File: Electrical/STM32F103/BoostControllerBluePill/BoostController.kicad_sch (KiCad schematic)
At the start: 60 parts, among them J1 PW-RPM-SPD-TPS, J2 OIL-WATER-AFR, J3 WG-FPUMP, J4 MAP-FPRES, J5 CAN, J6 GND_TP, J7 PROG, Q3 S9013, Q4 S9013, U1 YAAJ_BluePill_SWD_Breakout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

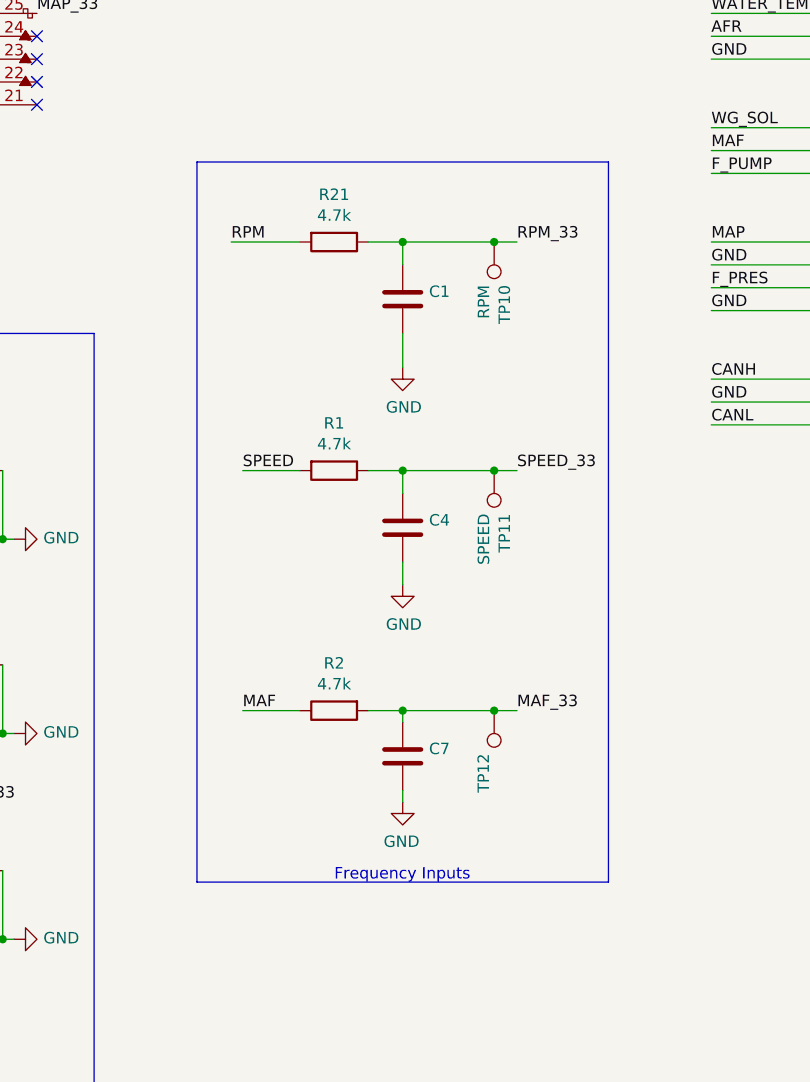
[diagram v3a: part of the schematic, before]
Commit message: [Electrical] Changed  frequency input voltage divider + filter rather than zener diode clamping.
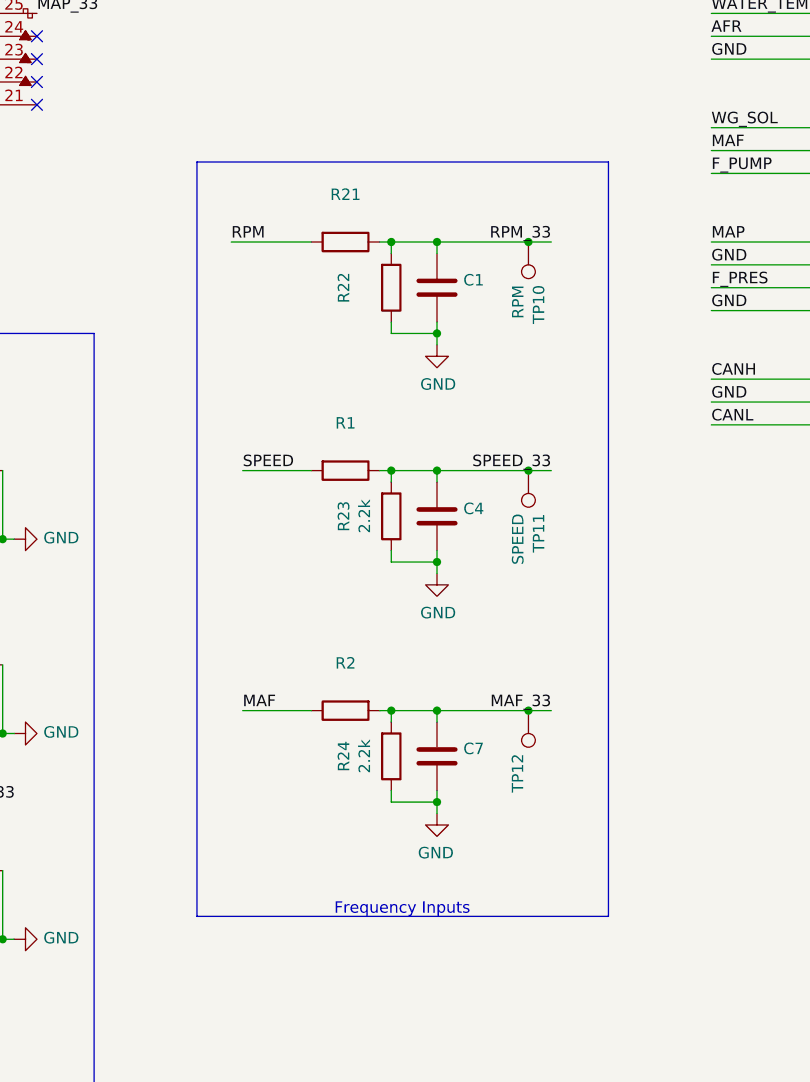
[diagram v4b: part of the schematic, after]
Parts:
- added R22: (no value), symbol Device:R
- added R23, R24: 2.2k, Resistor_SMD:R_1206_3216Metric_Pad1.30x1.75mm_HandSolder, symbol Device:R
- R1, R2, R21: value 4.7k -> (none); footprint Resistor_SMD:R_1206_3216Metric_Pad1.30x1.75mm_HandSolder -> (none)
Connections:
- net GND: now also R22.1, R23.1, R24.1
- net MAF_33: now also R24.2
- net RPM_33: now also R22.2
- net SPEED_33: now also R23.2
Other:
- moved on the sheet: C1, C4, C7, R1, R2, R21, TP10, TP11, TP12

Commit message: Added serial port support on dupond header for local data logging. Added missing MAF input resistor. Changed power transistor reference. Changed analog input voltage divisor values.
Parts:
- added J8: (no value), symbol Connector_Generic:Conn_01x03
- C1, C4, C7: value (none) -> 10n; footprint (none) -> Capacitor_SMD:C_0603_1608Metric_Pad1.08x0.95mm_HandSolder
- C10, C2, C3, C5, C6, C8, C9: value (none) -> 10µ; footprint (none) -> Capacitor_SMD:C_0603_1608Metric_Pad1.08x0.95mm_HandSolder
- Q1, Q2: value (none) -> IRF3205; footprint (none) -> Package_TO_SOT_THT:TO-220-3_Vertical
- R1, R11, R13, R15, R17, R19, R2, R21, R7, R9: value (none) -> 1.2k; footprint (none) -> Resistor_SMD:R_1206_3216Metric_Pad1.30x1.75mm_HandSolder
- R10, R12, R14, R16, R18, R20, R22, R8: value (none) -> 2.2k; footprint (none) -> Resistor_SMD:R_1206_3216Metric_Pad1.30x1.75mm_HandSolder
- TP12: value (none) -> MAF; footprint (none) -> TestPoint:TestPoint_Pad_D3.0mm
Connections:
- net GND: now also J8.2 (Pin_2)
- net TX: now reaches U1.14 (PB6)
- net TX: now also J8.1 (Pin_1)
- net RX: now reaches U1.15 (PB7)
- net RX: now also J8.3 (Pin_3)
- no-connect marks 23 -> 21

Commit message: Added CAN load resistor and jumper
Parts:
- added JP1: CAN load resistor, Connector_PinHeader_2.54mm:PinHeader_1x02_P2.54mm_Vertical, symbol Jumper:Jumper_2_Bridged
- added R25: 120, Resistor_SMD:R_1206_3216Metric_Pad1.30x1.75mm_HandSolder, symbol Device:R
- J8: value (none) -> SERIAL; footprint (none) -> Connector_PinHeader_2.54mm:PinHeader_1x03_P2.54mm_Vertical
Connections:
- net CANH: now also JP1.1 (A)
- net CANL: now also R25.1
- new net: JP1.2 (B), R25.2
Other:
- note added: "Analog Inputs"
- moved on the sheet: U3
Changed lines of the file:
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@@
     (stroke (width 0) (type default) (color 0 0 0 0))
   )
-  (wire (pts (xy 49.53 148.59) (xy 49.53 152.4))
+  (wire (pts (xy 43.18 151.13) (xy 43.18 154.94))
     (stroke (width 0) (type default) (color 0 0 0 0))
   )
@@
     (stroke (width 0) (type default) (color 0 0 0 0))
   )
-  (wire (pts (xy 46.99 148.59) (xy 46.99 152.4))
+  (wire (pts (xy 40.64 151.13) (xy 40.64 154.94))
     (stroke (width 0) (type default) (color 0 0 0 0))
   )
@@
     (stroke (width 0) (type default) (color 0 0 0 0))
   )
+  (wire (pts (xy 76.2 165.1) (xy 76.2 170.18))
+    (stroke (width 0) (type default) (color 0 0 0 0))
+  )
   (wire (pts (xy 153.67 119.38) (xy 163.83 119.38))
     (stroke (width 0) (type default) (color 0 0 0 0))
@@
     (stroke (width 0) (type default) (color 0 0 0 0))
   )
-  (wire (pts (xy 60.96 165.1) (xy 68.58 165.1))
+  (wire (pts (xy 54.61 167.64) (xy 64.77 167.64))
     (stroke (width 0) (type default) (color 0 0 0 0))
   )
@@
     (stroke (width 0) (type default) (color 0 0 0 0))
   )
+  (wire (pts (xy 76.2 170.18) (xy 74.93 170.18))
+    (stroke (width 0) (type default) (color 0 0 0 0))
+  )
   (wire (pts (xy 212.09 148.59) (xy 212.09 149.86))
     (stroke (width 0) (type default) (color 0 0 0 0))
@@
     (stroke (width 0) (type default) (color 0 0 0 0))
   )
+  (wire (pts (xy 67.31 170.18) (xy 64.77 170.18))
+    (stroke (width 0) (type default) (color 0 0 0 0))
+  )
   (wire (pts (xy 49.53 127) (xy 29.21 127))
     (stroke (width 0) (type default) (color 0 0 0 0))
@@
     (stroke (width 0) (type default) (color 0 0 0 0))
   )
-  (wire (pts (xy 26.67 165.1) (xy 35.56 165.1))
+  (wire (pts (xy 20.32 167.64) (xy 29.21 167.64))
     (stroke (width 0) (type default) (color 0 0 0 0))
   )
@@
     (stroke (width 0) (type default) (color 0 0 0 0))
   )
+  (wire (pts (xy 64.77 170.18) (xy 64.77 167.64))
+    (stroke (width 0) (type default) (color 0 0 0 0))
+  )
   (polyline (pts (xy 173.99 191.77) (xy 82.55 191.77))
     (stroke (width 0) (type default) (color 0 0 0 0))
@@
     (stroke (width 0) (type default) (color 0 0 0 0))
   )
-  (wire (pts (xy 26.67 162.56) (xy 35.56 162.56))
+  (wire (pts (xy 20.32 165.1) (xy 29.21 165.1))
     (stroke (width 0) (type default) (color 0 0 0 0))
   )
@@
     (stroke (width 0) (type default) (color 0 0 0 0))
   )
-  (wire (pts (xy 60.96 162.56) (xy 68.58 162.56))
+  (wire (pts (xy 54.61 165.1) (xy 66.04 165.1))
     (stroke (width 0) (type default) (color 0 0 0 0))
   )
@@
   )
   (text "Frequency Inputs" (at 200.66 161.29 0)
+    (effects (font (size 1.27 1.27)) (justify left bottom))
+  )
+  (text "Analog Inputs" (at 121.92 191.77 0)
     (effects (font (size 1.27 1.27)) (justify left bottom))
   )
@@
     (effects (font (size 1.27 1.27)) (justify right bottom))
   )
-  (label "CAN_TX" (at 26.67 162.56 0)
+  (label "CAN_TX" (at 20.32 165.1 0)
     (effects (font (size 1.27 1.27)) (justify left bottom))
   )
@@
     (effects (font (size 1.27 1.27)) (justify left bottom))
   )
-  (label "CANL" (at 68.58 165.1 180)
+  (label "CANL" (at 62.23 167.64 180)
     (effects (font (size 1.27 1.27)) (justify right bottom))
   )
@@
     (effects (font (size 1.27 1.27)) (justify right bottom))
   )
-  (label "+5V" (at 46.99 148.59 90)
+  (label "+5V" (at 40.64 151.13 90)
     (effects (font (size 1.27 1.27)) (justify left bottom))
   )
@@
     (effects (font (size 1.27 1.27)) (justify left bottom))
   )
-  (label "CANH" (at 68.58 162.56 180)
+  (label "CANH" (at 62.23 165.1 180)
     (effects (font (size 1.27 1.27)) (justify right bottom))
   )
-  (label "CAN_RX" (at 26.67 165.1 0)
+  (label "CAN_RX" (at 20.32 167.64 0)
     (effects (font (size 1.27 1.27)) (justify left bottom))
   )
@@
     (pin "1")
   )
-  (symbol (lib_id "BoostController-rescue:MCP2551_MODULE-sonix") (at 48.26 163.83 0) (unit 1)
-    (in_bom yes) (on_board yes)
-    (property "Reference" "U3" (id 0) (at 48.26 174.5742 0))
-    (property "Value" "MCP2551_MODULE" (id 1) (at 48.26 176.8856 0))
-    (property "Footprint" "Sonix:MCP2551_MODULE" (id 2) (at 48.26 173.99 0)
-      (effects (font (size 1.27 1.27)) hide)
-    )
-    (property "Datasheet" "" (id 3) (at 44.45 162.56 0)
+  (symbol (lib_id "BoostController-rescue:MCP2551_MODULE-sonix") (at 41.91 166.37 0) (unit 1)
+    (in_bom yes) (on_board yes)
+    (property "Reference" "U3" (id 0) (at 41.91 177.1142 0))
+    (property "Value" "MCP2551_MODULE" (id 1) (at 41.91 179.4256 0))
+    (property "Footprint" "Sonix:MCP2551_MODULE" (id 2) (at 41.91 176.53 0)
+      (effects (font (size 1.27 1.27)) hide)
+    )
+    (property "Datasheet" "" (id 3) (at 38.1 165.1 0)
       (effects (font (size 1.27 1.27)) hide)
     )
@@
     (pin "6")
   )
-  (symbol (lib_id "power:GND") (at 49.53 148.59 180) (unit 1)
-    (in_bom yes) (on_board yes)
-    (property "Reference" "#PWR02" (id 0) (at 49.53 142.24 0)
-      (effects (font (size 1.27 1.27)) hide)
-    )
-    (property "Value" "GND" (id 1) (at 49.403 144.1958 0))
-    (property "Footprint" "" (id 2) (at 49.53 148.59 0)
-      (effects (font (size 1.27 1.27)) hide)
-    )
-    (property "Datasheet" "" (id 3) (at 49.53 148.59 0)
+  (symbol (lib_id "power:GND") (at 43.18 151.13 180) (unit 1)
+    (in_bom yes) (on_board yes)
+    (property "Reference" "#PWR02" (id 0) (at 43.18 144.78 0)
+      (effects (font (size 1.27 1.27)) hide)
+    )
+    (property "Value" "GND" (id 1) (at 43.053 146.7358 0))
+    (property "Footprint" "" (id 2) (at 43.18 151.13 0)
+      (effects (font (size 1.27 1.27)) hide)
+    )
+    (property "Datasheet" "" (id 3) (at 43.18 151.13 0)
       (effects (font (size 1.27 1.27)) hide)
     )
@@
     (pin "1")
   )
+  (symbol (lib_id "Device:R") (at 71.12 170.18 90) (unit 1)
+    (in_bom yes) (on_board yes)
+    (property "Reference" "R25" (id 0) (at 71.12 172.72 90))
+    (property "Value" "120" (id 1) (at 71.12 168.0011 90))
+    (property "Footprint" "Resistor_SMD:R_1206_3216Metric_Pad1.30x1.75mm_HandSolder" (id 2) (at 71.12 171.958 90)
+      (effects (font (size 1.27 1.27)) hide)
+    )
+    (property "Datasheet" "~" (id 3) (at 71.12 170.18 0)
+      (effects (font (size 1.27 1.27)) hide)
+    )
+    (pin "1")
+    (pin "2")
+  )
   (symbol (lib_id "Connector:TestPoint") (at 222.25 111.76 180) (unit 1)
     (in_bom yes) (on_board yes)
@@
       (effects (font (size 1.27 1.27)) (justify left))
     )
-    (property "Value" "" (id 1) (at 220.472 34.2646 0)
-      (effects (font (size 1.27 1.27)) (justify left))
-    )
-    (property "Footprint" "" (id 2) (at 218.44 33.02 0)
+    (property "Value" "SERIAL" (id 1) (at 220.472 34.2646 0)
+      (effects (font (size 1.27 1.27)) (justify left))
+    )
+    (property "Footprint" "Connector_PinHeader_2.54mm:PinHeader_1x03_P2.54mm_Vertical" (id 2) (at 218.44 33.02 0)
       (effects (font (size 1.27 1.27)) hide)
     )
@@
     (pin "2")
   )
+  (symbol (lib_id "Jumper:Jumper_2_Bridged") (at 71.12 165.1 0) (unit 1)
+    (in_bom yes) (on_board yes) (fields_autoplaced)
+    (property "Reference" "JP1" (id 0) (at 71.12 160.7652 0))
+    (property "Value" "CAN load resistor" (id 1) (at 71.12 163.3021 0))
+    (property "Footprint" "Connector_PinHeader_2.54mm:PinHeader_1x02_P2.54mm_Vertical" (id 2) (at 71.12 165.1 0)
+      (effects (font (size 1.27 1.27)) hide)
+    )
+    (property "Datasheet" "~" (id 3) (at 71.12 165.1 0)
+      (effects (font (size 1.27 1.27)) hide)
+    )
+    (pin "1")
+    (pin "2")
+  )
   (symbol (lib_id "Device:R") (at 207.01 91.44 0) (mirror x) (unit 1)
     (in_bom yes) (on_board yes)
@@
       (reference "J8") (unit 1) (value "SERIAL") (footprint "Connector_PinHeader_2.54mm:PinHeader_1x03_P2.54mm_Vertical")
     )
+    (path "/d1223fbe-eaba-4d52-95ce-58acb7d0da1e"
+      (reference "JP1") (unit 1) (value "CAN load resistor") (footprint "Connector_PinHeader_2.54mm:PinHeader_1x02_P2.54mm_Vertical")
+    )
     (path "/00000000-0000-0000-0000-0000618d77dc"
       (reference "Q1") (unit 1) (value "IRF3205") (footprint "Package_TO_SOT_THT:TO-220-3_Vertical")
@@
       (reference "R24") (unit 1) (value "2.2k") (footprint "Resistor_SMD:R_1206_3216Metric_Pad1.30x1.75mm_HandSolder")
     )
+    (path "/60c86474-78a5-480b-8a3a-6f5de68abac0"
+      (reference "R25") (unit 1) (value "120") (footprint "Resistor_SMD:R_1206_3216Metric_Pad1.30x1.75mm_HandSolder")
+    )
     (path "/00000000-0000-0000-0000-000061b56ad1"

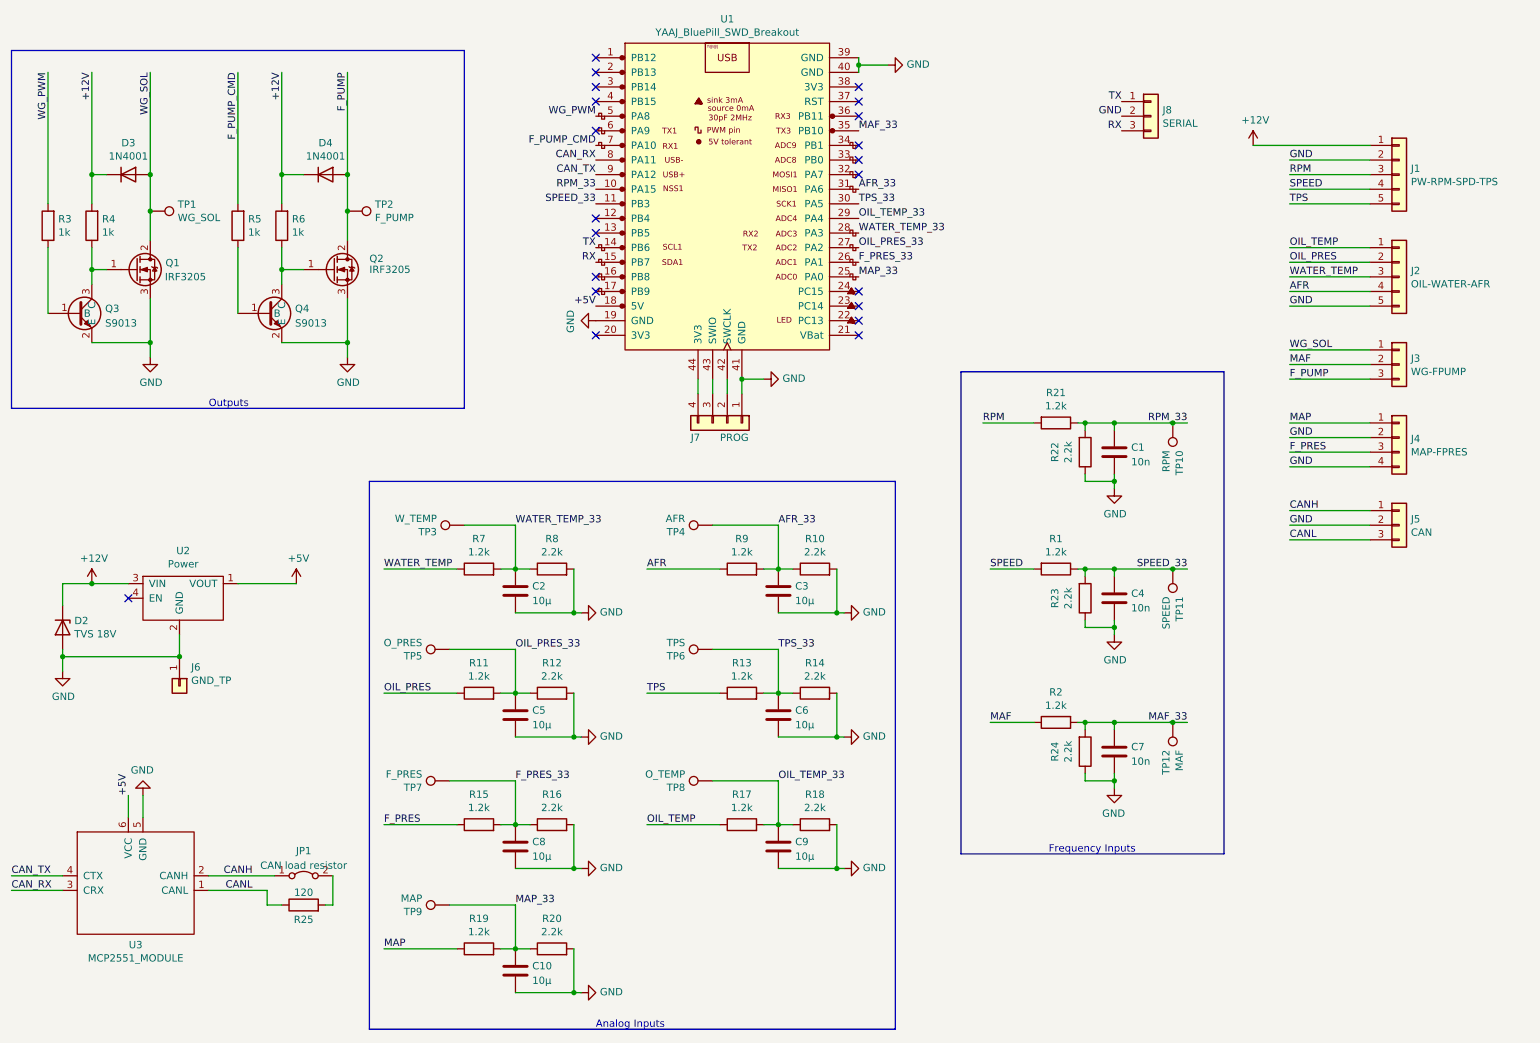
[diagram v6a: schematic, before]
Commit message: Added OP Amp on analog inputs Split schematics with sub schematic for analog inputs.
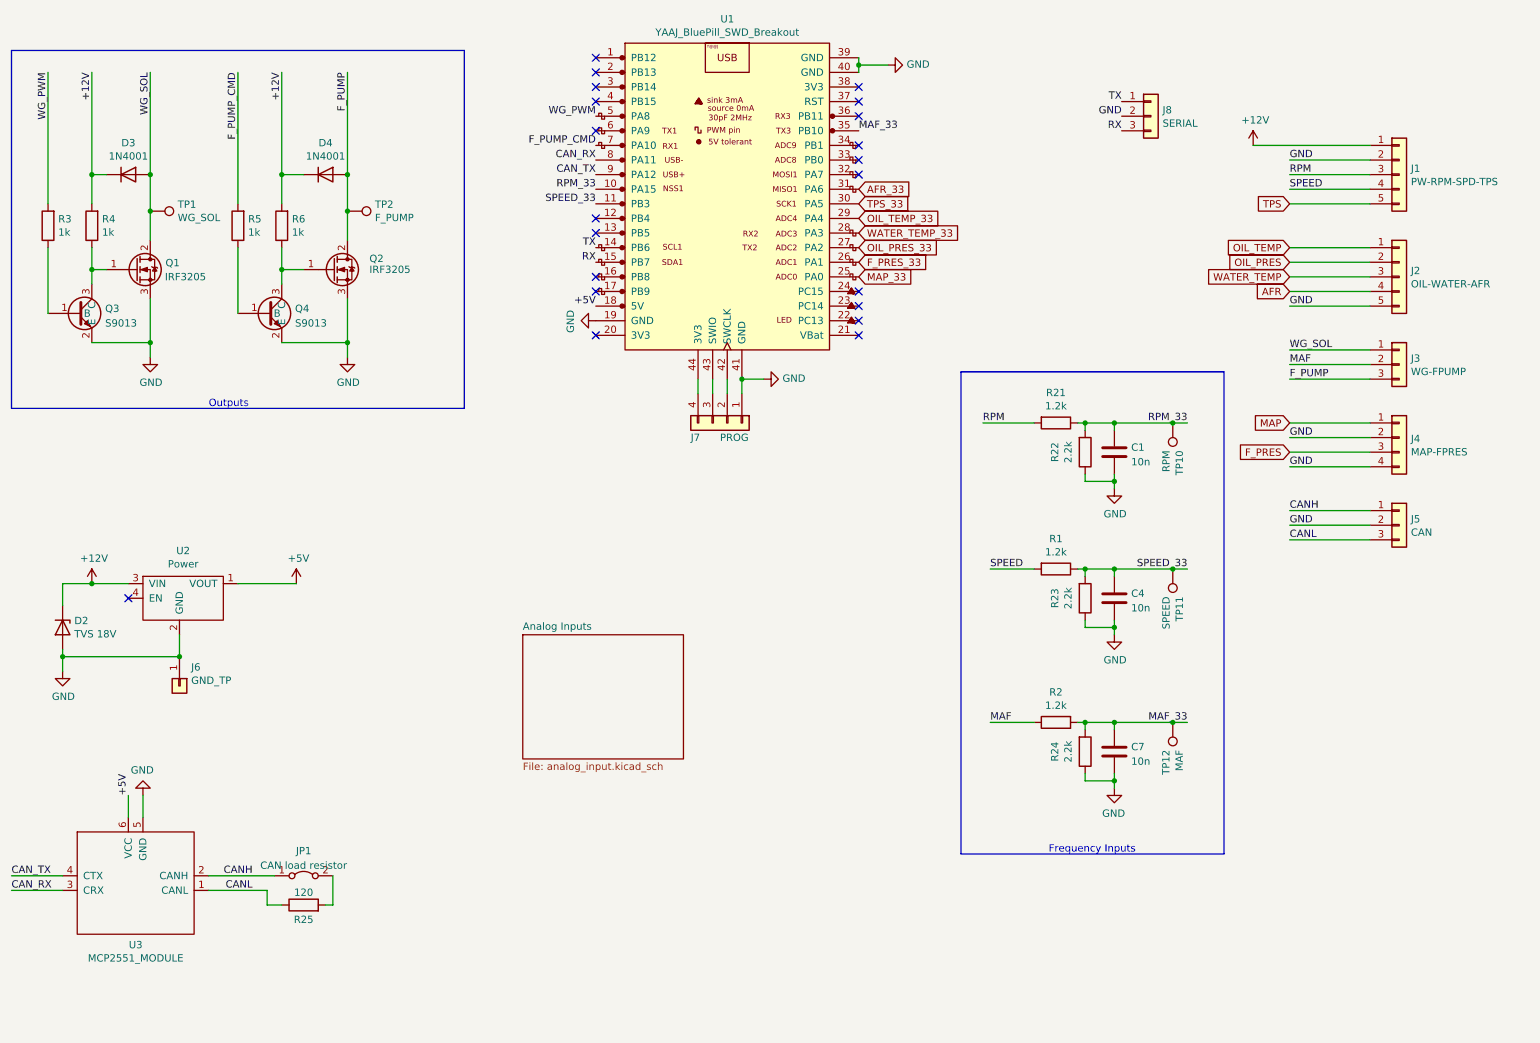
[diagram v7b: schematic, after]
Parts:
- removed C10, C2, C3, C5, C6, C8, C9: 10µ, Capacitor_SMD:C_0603_1608Metric_Pad1.08x0.95mm_HandSolder, symbol Device:C
- removed R10, R12, R14, R16, R18, R20, R8: 2.2k, Resistor_SMD:R_1206_3216Metric_Pad1.30x1.75mm_HandSolder, symbol Device:R
- removed R11, R13, R15, R17, R19, R7, R9: 1.2k, Resistor_SMD:R_1206_3216Metric_Pad1.30x1.75mm_HandSolder, symbol Device:R
- removed TP3: W_TEMP, Measurement_Points:Measurement_Point_Round-SMD-Pad_Big, symbol Connector:TestPoint
- removed TP4: AFR, Measurement_Points:Measurement_Point_Round-SMD-Pad_Big, symbol Connector:TestPoint
- removed TP5: O_PRES, Measurement_Points:Measurement_Point_Round-SMD-Pad_Big, symbol Connector:TestPoint
- removed TP6: TPS, Measurement_Points:Measurement_Point_Round-SMD-Pad_Big, symbol Connector:TestPoint
- removed TP7: F_PRES, Measurement_Points:Measurement_Point_Round-SMD-Pad_Big, symbol Connector:TestPoint
- removed TP8: O_TEMP, Measurement_Points:Measurement_Point_Round-SMD-Pad_Big, symbol Connector:TestPoint
- removed TP9: MAP, Measurement_Points:Measurement_Point_Round-SMD-Pad_Big, symbol Connector:TestPoint
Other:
- added sheet Analog Inputs (analog_input.kicad_sch)
- note removed: "Analog Inputs"
